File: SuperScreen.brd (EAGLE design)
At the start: 32.3 x 37.7 mm, 30 parts, among them CN2 JSTPH, CN3 1X4-BIG, IC2 MIC5225, Q3 BSS138, U2 MCP73831T-2ACI/OT

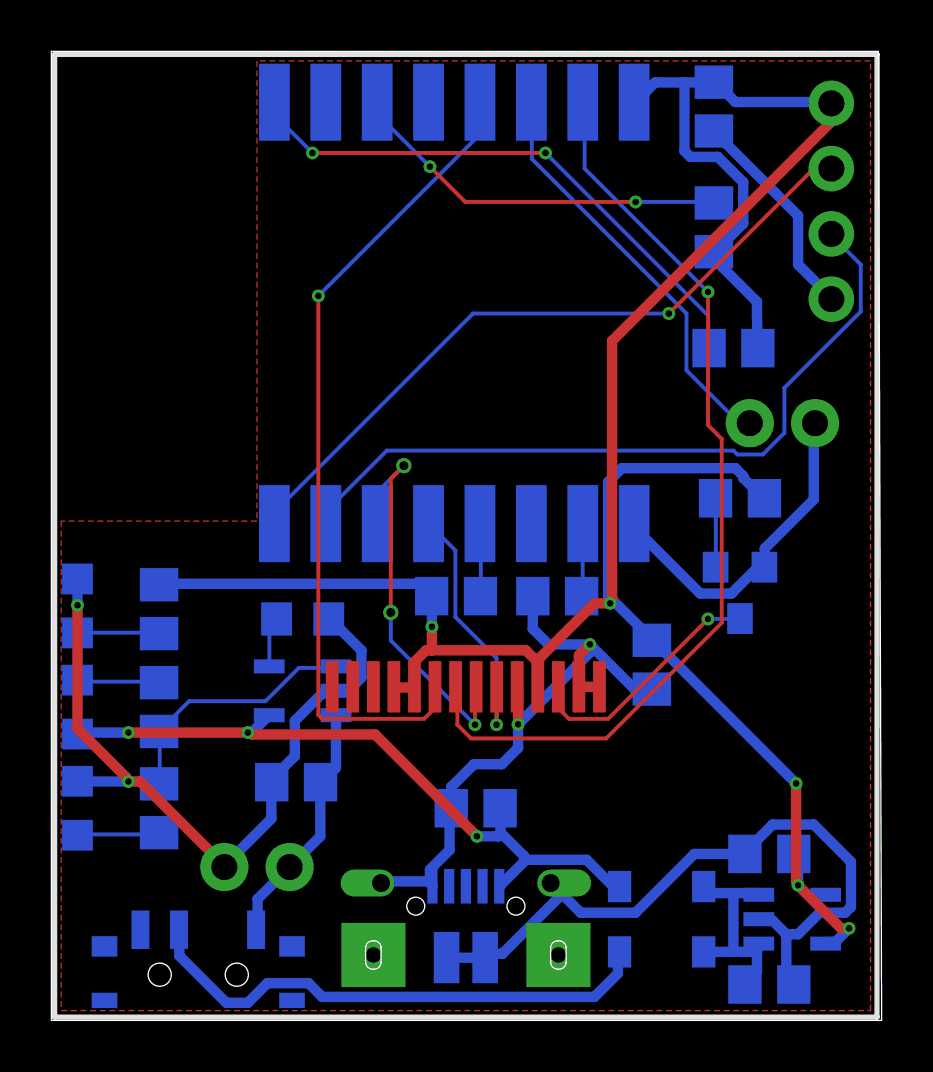
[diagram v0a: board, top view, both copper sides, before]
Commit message: Adding in new usb connector
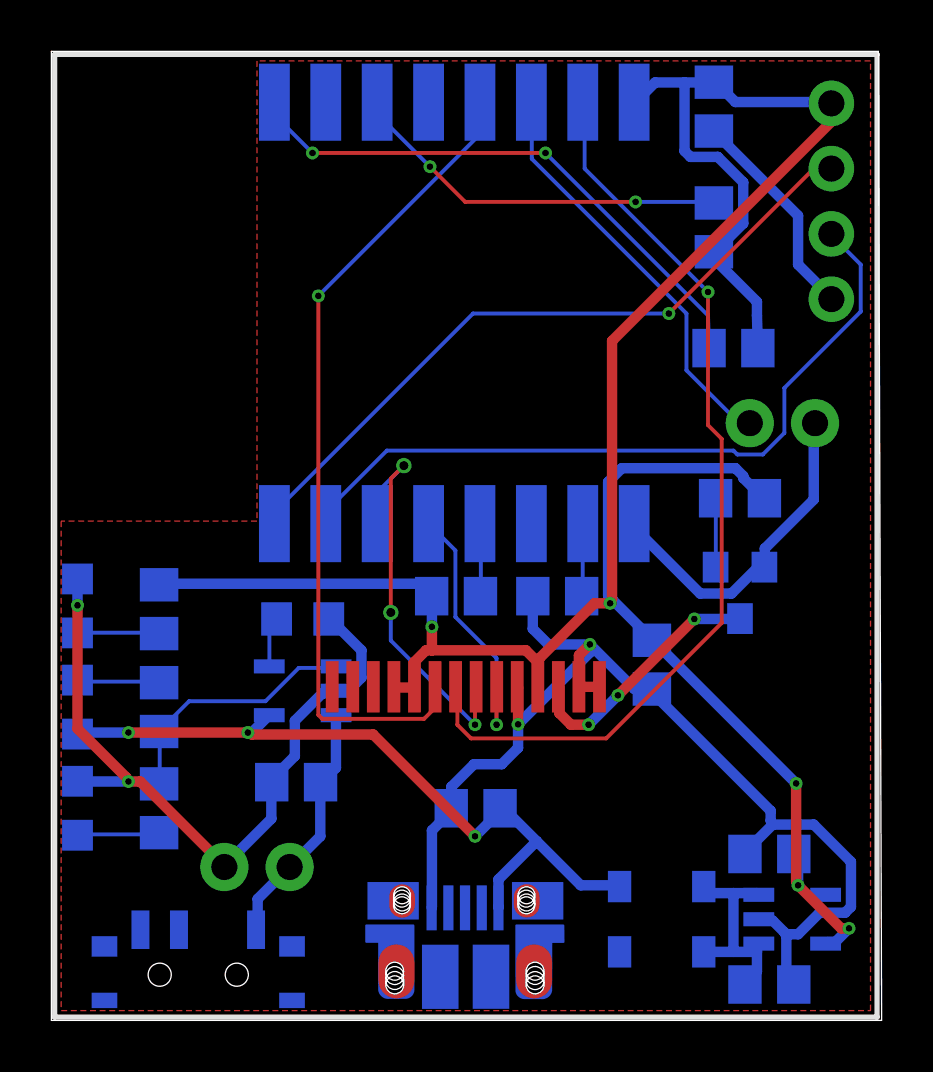
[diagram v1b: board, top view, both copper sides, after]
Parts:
- CN1: value (none) -> AMP FCI 10103594-0001LF; device microbuilder:4UCONN_20329 -> SparkFun-Connectors:USB-MICROB-PTH
- moved CN1 1.40 mm to (59.7, 19.4)
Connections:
- net N$5 renamed LED-
- removed net N$7: TFT2.12
- net CS: now also TFT2.12
- net GND: no longer CN1.BASE@1, CN1.BASE@2, CN1.SPRT@1, CN1.SPRT@2, CN1.SPRT@3, CN1.SPRT@4
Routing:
- net N$3: track 20.7 -> 0.00 mm
- net GND: track 104.2 -> 95.6 mm
- net VBUS: track 27.3 -> 28.9 mm
- net LED-: track 9.69 -> 9.97 mm, vias 1 -> 3

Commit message: Added some gnd vias about to run the autorouter again
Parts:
- moved C8 5.50 mm to (63.4, 26.0), turned to 180 degrees
- moved R10 1.97 mm to (65.2, 32.9), turned to 180 degrees
- moved C3 1.15 mm to (58.9, 24.5)
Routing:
- net +3V3: track 100.0 -> 0.00 mm, vias 5 -> 0
- net GND: track 95.6 -> 0.00 mm, vias 4 -> 11
- net MOSI: track 36.4 -> 0.00 mm, vias 1 -> 0
- net SCK: track 32.1 -> 0.00 mm, vias 1 -> 0
- net RX: track 29.2 -> 0.00 mm
- net VBUS: track 28.9 -> 0.00 mm, vias 3 -> 0
- net TX: track 27.7 -> 0.00 mm, vias 1 -> 0
- net N$2: track 21.9 -> 0.00 mm, vias 2 -> 0
- net N$6: track 16.2 -> 0.00 mm
- net TFTDC: track 15.8 -> 0.00 mm, vias 3 -> 0
- net N$15: track 15.0 -> 0.00 mm, vias 2 -> 0
- net TFTRESET: track 10.4 -> 0.00 mm, vias 1 -> 0
- net N$4: track 10.0 -> 0.00 mm
- net LED-: track 9.97 -> 0.00 mm, vias 3 -> 0
- net VBAT: track 9.65 -> 0.00 mm
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
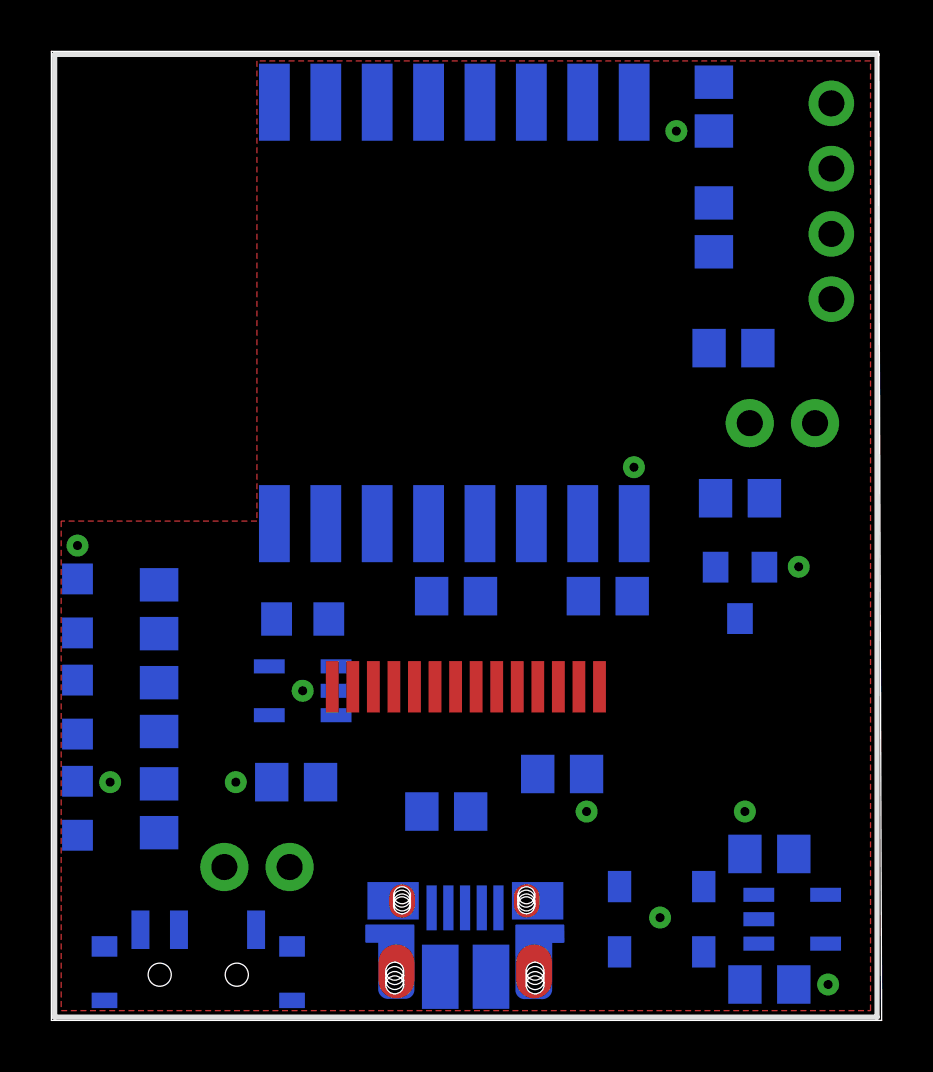
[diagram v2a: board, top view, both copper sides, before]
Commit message: R1 Ordered from OshPark
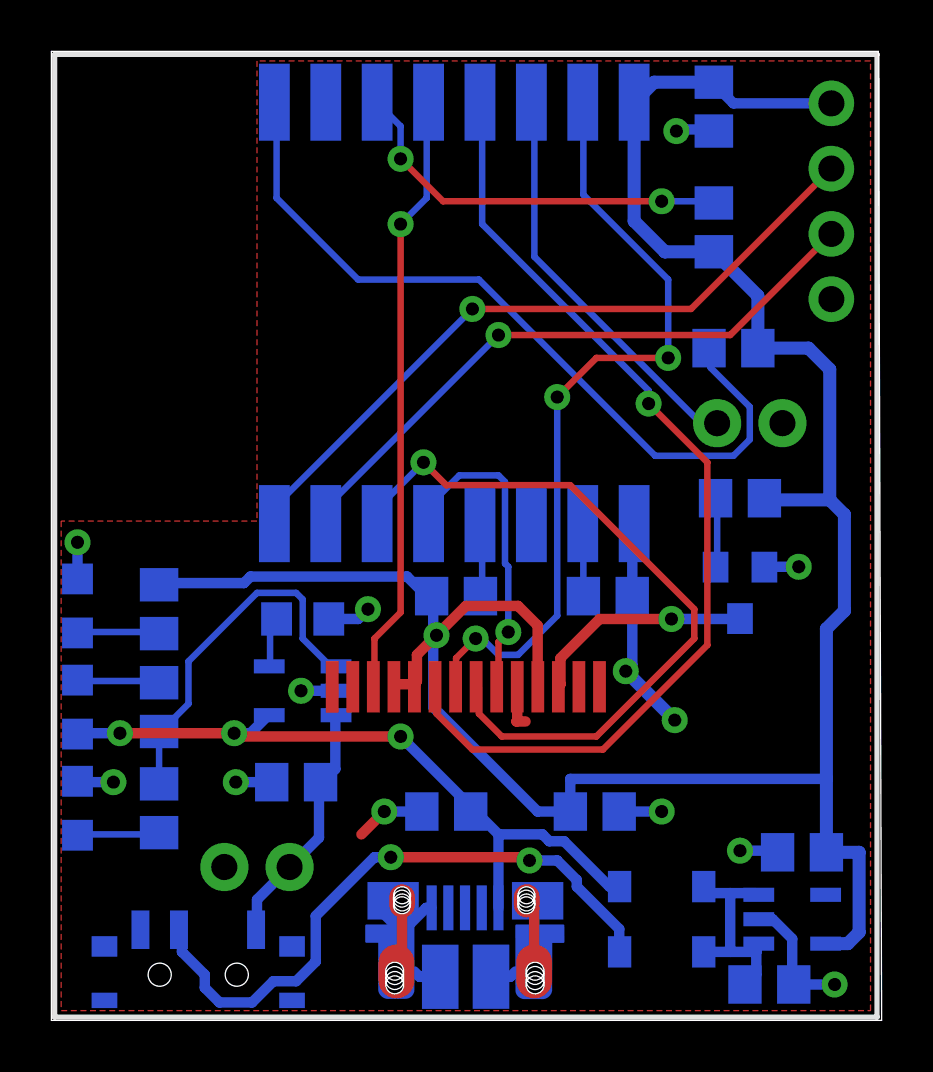
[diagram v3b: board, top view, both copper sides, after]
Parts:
- moved C8 1.94 mm to (64.7, 24.5)
- moved C2 1.27 mm to (72.8, 22.9)
- moved J1 1.27 mm to (72.0, 39.6)
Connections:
- net GND: now also CN1.P$1, CN1.P$10, CN1.P$12, CN1.P$2, CN1.P$3, CN1.P$4, CN1.P$6, CN1.P$8, CN1.SHEILD2, CN1.SHIELD, CN1.SHIELD3, CN1.SHIELD4
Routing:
- net +3V3: track 0.00 -> 96.2 mm, vias 0 -> 1
- net GND: track 0.00 -> 47.7 mm, vias 11 -> 13
- net SCK: track 0.00 -> 38.7 mm, vias 0 -> 1
- net MOSI: track 0.00 -> 31.0 mm, vias 0 -> 3
- net N$2: track 0.00 -> 30.9 mm
- net TFTDC: track 0.00 -> 28.6 mm, vias 0 -> 1
- net VBUS: track 0.00 -> 28.3 mm, vias 0 -> 3
- net TX: track 0.00 -> 27.8 mm, vias 0 -> 1
- net RX: track 0.00 -> 24.7 mm, vias 0 -> 1
- net N$3: track 0.00 -> 24.6 mm, vias 0 -> 2
- net CS: track 0.00 -> 23.6 mm, vias 0 -> 1
- net N$6: track 0.00 -> 15.9 mm
- net N$15: track 0.00 -> 15.5 mm, vias 0 -> 2
- net N$4: track 0.00 -> 14.2 mm
- net TFTRESET: track 0.00 -> 12.5 mm, vias 0 -> 1
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
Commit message: Use adafruit's 0805 resistors
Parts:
- R1, R10, R2, R3, R5, R6, R7, R8: device microbuilder:0805-NO -> adafruit:R0805
- R4: device microbuilder:_0805MP -> adafruit:R0805

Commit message: Use Adafruit 0805 caps
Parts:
- C2, C3, C4, C5, C6, C8: device microbuilder:0805-NO -> adafruit:C0805
